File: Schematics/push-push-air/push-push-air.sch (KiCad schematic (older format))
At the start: 6 parts

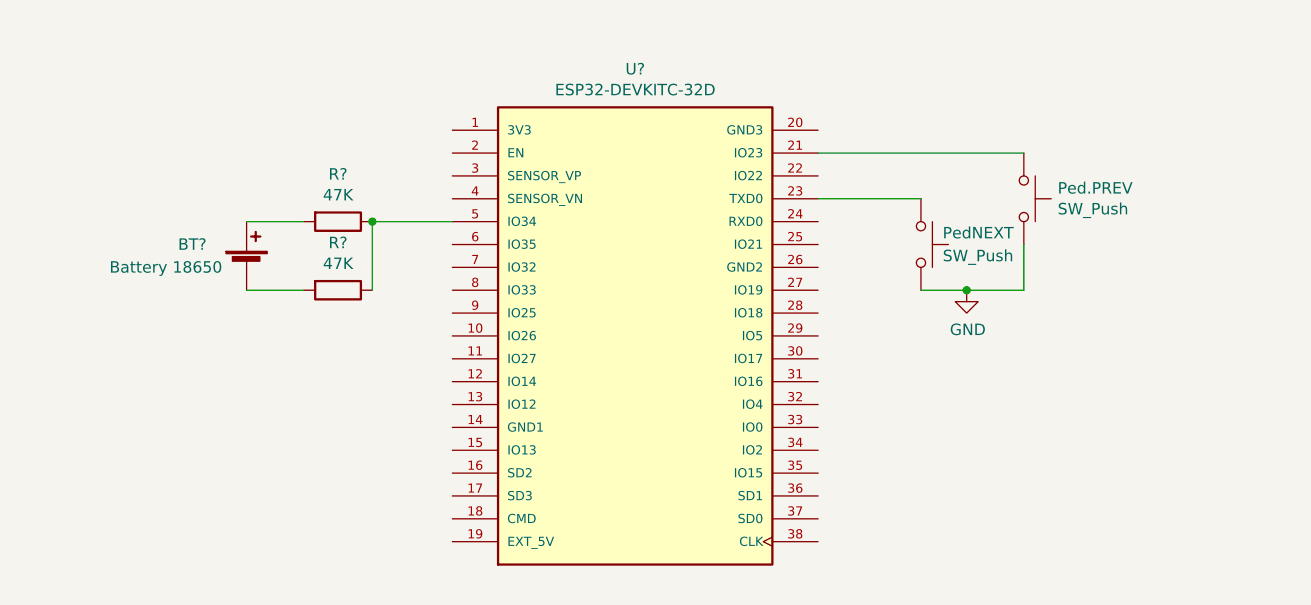
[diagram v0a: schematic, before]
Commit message: Update the schematics to align them to the current scketch
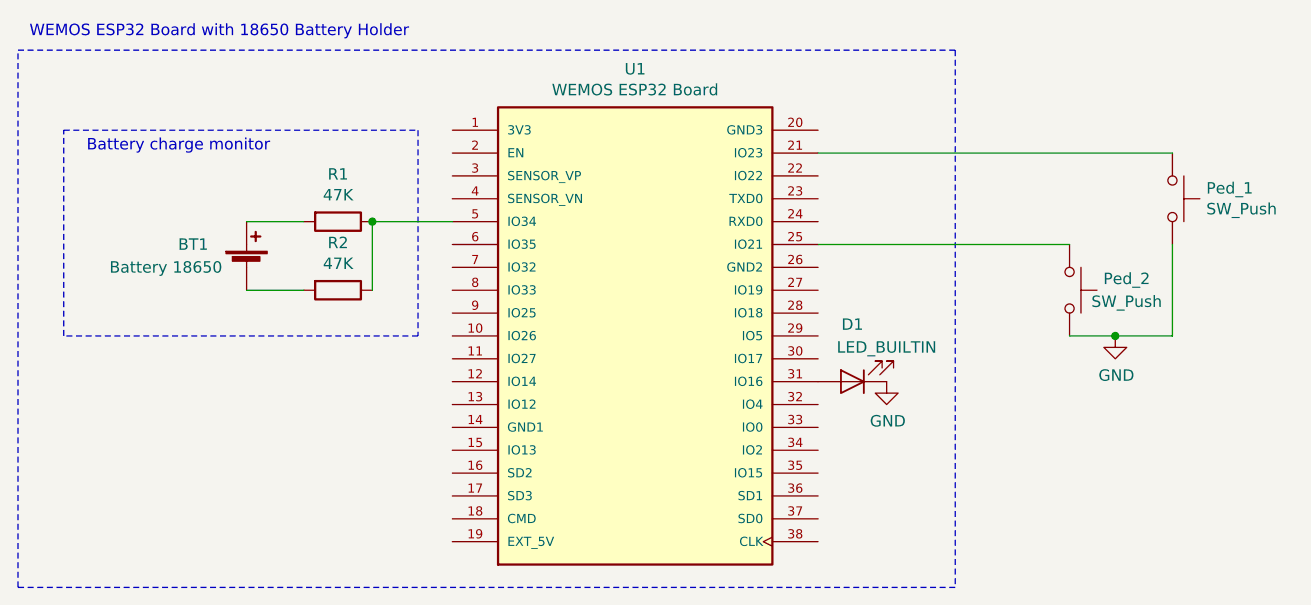
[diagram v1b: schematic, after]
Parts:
- added D1: LED_BUILTIN, symbol Device:LED
- U1: renamed from U?; value ESP32-DEVKITC-32D -> WEMOS ESP32 Board
- gave numbers to parts that had none: 3
- renumbered Ped.PREV to Ped_1, PedNEXT to Ped_2
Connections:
- net GND: now also D1.1 (K)
- net at U1.23 (TXD0): no longer Ped_2.1
- net at U1.25 (IO21): now also Ped_2.1
- net at U1.31 (IO16): now also D1.2 (A)
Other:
- note added: "Battery charge monitor"
- note added: "WEMOS ESP32 Board with 18650 Battery Holder"
- moved on the sheet: Ped_1, Ped_2
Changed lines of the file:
@@
 EESchema Schematic File Version 4
+LIBS:push-push-air-cache
 EELAYER 29 0
 EELAYER END
@@
 encoding utf-8
 Sheet 1 1
-Title "Push Push Air"
-Date "2021-08-01"
-Rev "ver 1.0"
+Title "Push Push Air 2"
+Date "2022-04-28"
+Rev "ver 2.o"
 Comp "UBI Stage"
 Comment1 ""
@@
 $EndDescr
 $Comp
-L ESP32-DEVKITC-32D:ESP32-DEVKITC-32D U?
+L ESP32-DEVKITC-32D:ESP32-DEVKITC-32D U1
 U 1 1 623A0D71
 P 5550 3850
-F 0 "U?" H 5550 5017 50  0000 C CNN
-F 1 "ESP32-DEVKITC-32D" H 5550 4926 50  0000 C CNN
+F 0 "U1" H 5550 5017 50  0000 C CNN
+F 1 "WEMOS ESP32 Board" H 5550 4926 50  0000 C CNN
 F 2 "MODULE_ESP32-DEVKITC-32D" H 5550 3850 50  0001 L BNN
 F 3 "" H 5550 3850 50  0001 L BNN
@@
 $EndComp
 $Comp
-L Device:R R?
+L Device:R R2
 U 1 1 623A29FF
 P 4250 3650
-F 0 "R?" V 4043 3650 50  0000 C CNN
+F 0 "R2" V 4043 3650 50  0000 C CNN
 F 1 "47K" V 4134 3650 50  0000 C CNN
 F 2 "" V 4180 3650 50  0001 C CNN
@@
 $EndComp
 $Comp
-L Device:R R?
+L Device:R R1
 U 1 1 623A32C7
 P 4250 3350
-F 0 "R?" V 4043 3350 50  0000 C CNN
+F 0 "R1" V 4043 3350 50  0000 C CNN
 F 1 "47K" V 4134 3350 50  0000 C CNN
 F 2 "" V 4180 3350 50  0001 C CNN
@@
 $EndComp
 $Comp
-L Switch:SW_Push PedNEXT
+L Switch:SW_Push Ped_2
 U 1 1 623A22F1
-P 6800 3450
-F 0 "PedNEXT" V 6750 3700 50  0000 C CNN
-F 1 "SW_Push" V 6850 3700 50  0000 C CNN
-F 2 "" H 6800 3650 50  0001 C CNN
-F 3 "~" H 6800 3650 50  0001 C CNN
-	1    6800 3450
+P 7450 3650
+F 0 "Ped_2" V 7400 3900 50  0000 C CNN
+F 1 "SW_Push" V 7500 3900 50  0000 C CNN
+F 2 "" H 7450 3850 50  0001 C CNN
+F 3 "~" H 7450 3850 50  0001 C CNN
+	1    7450 3650
 	0    1    1    0
 $EndComp
 $Comp
-L Switch:SW_Push Ped.PREV
+L Switch:SW_Push Ped_1
 U 1 1 623A23D3
-P 7250 3250
-F 0 "Ped.PREV" V 7204 3398 50  0000 L CNN
-F 1 "SW_Push" V 7295 3398 50  0000 L CNN
-F 2 "" H 7250 3450 50  0001 C CNN
-F 3 "~" H 7250 3450 50  0001 C CNN
-	1    7250 3250
+P 7900 3250
+F 0 "Ped_1" V 7854 3398 50  0000 L CNN
+F 1 "SW_Push" V 7945 3398 50  0000 L CNN
+F 2 "" H 7900 3450 50  0001 C CNN
+F 3 "~" H 7900 3450 50  0001 C CNN
+	1    7900 3250
 	0    1    1    0
 $EndComp
 $Comp
-L Device:Battery_Cell BT?
+L Device:Battery_Cell BT1
 U 1 1 623A8D9A
 P 3850 3550
-F 0 "BT?" H 3550 3650 50  0000 L CNN
+F 0 "BT1" H 3550 3650 50  0000 L CNN
 F 1 "Battery 18650" H 3250 3550 50  0000 L CNN
 F 2 "" V 3850 3610 50  0001 C CNN
@@
 	4100 3350 3850 3350
 Wire Wire Line
-	6350 3050 7250 3050
-Wire Wire Line
-	6350 3250 6800 3250
-Wire Wire Line
-	6800 3650 7000 3650
-Wire Wire Line
-	7250 3650 7250 3450
+	7450 3850 7650 3850
 $Comp
 L power:GND #PWR?
 U 1 1 623AE0F7
-P 7000 3650
-F 0 "#PWR?" H 7000 3400 50  0001 C CNN
-F 1 "GND" H 7005 3477 50  0000 C CNN
-F 2 "" H 7000 3650 50  0001 C CNN
-F 3 "" H 7000 3650 50  0001 C CNN
-	1    7000 3650
+P 7650 3850
+F 0 "#PWR?" H 7650 3600 50  0001 C CNN
+F 1 "GND" H 7655 3677 50  0000 C CNN
+F 2 "" H 7650 3850 50  0001 C CNN
+F 3 "" H 7650 3850 50  0001 C CNN
+	1    7650 3850
 	1    0    0    -1
 $EndComp
-Connection ~ 7000 3650
+Connection ~ 7650 3850
 Wire Wire Line
-	7000 3650 7250 3650
+	7650 3850 7900 3850
+$Comp
+L Device:LED D1
+U 1 1 626A715F
+P 6500 4050
+F 0 "D1" H 6500 3800 50  0000 C CNN
+F 1 "LED_BUILTIN" H 6350 3900 50  0000 C CNN
+F 2 "" H 6500 4050 50  0001 C CNN
+F 3 "~" H 6500 4050 50  0001 C CNN
+	1    6500 4050
+	-1   0    0    1
+$EndComp
+$Comp
+L power:GND #PWR?
+U 1 1 626A7B0B
+P 6650 4050
+F 0 "#PWR?" H 6650 3800 50  0001 C CNN
+F 1 "GND" H 6655 3877 50  0000 C CNN
+F 2 "" H 6650 4050 50  0001 C CNN
+F 3 "" H 6650 4050 50  0001 C CNN
+	1    6650 4050
+	1    0    0    -1
+$EndComp
+Wire Notes Line
+	4600 2950 4600 3850
+Wire Notes Line
+	4600 3850 3050 3850
+Wire Notes Line
+	3050 3850 3050 2950
+Wire Notes Line
+	3050 2950 4600 2950
+Text Notes 3150 3050 0    50   ~ 0
+Battery charge monitor
+Wire Notes Line
+	2850 2600 6950 2600
+Wire Notes Line
+	6950 2600 6950 4950
+Wire Notes Line
+	6950 4950 2850 4950
+Wire Notes Line
+	2850 4950 2850 2600
+Text Notes 2900 2550 0    50   ~ 0
+WEMOS ESP32 Board with 18650 Battery Holder
+Wire Wire Line
+	6350 3050 7900 3050
+Wire Wire Line
+	7900 3450 7900 3850
+Wire Wire Line
+	6350 3450 7450 3450
 $EndSCHEMATC
